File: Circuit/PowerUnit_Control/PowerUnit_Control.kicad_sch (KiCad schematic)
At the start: 25 parts, among them J1 Conn_01x02_Pin, J10 Conn_01x02_Pin, J11 Conn_01x02_Pin, J2 Conn_01x02_Pin, J3 Conn_01x07_Socket, J4 Conn_01x02_Pin, J5 Conn_01x02_Pin, J6 Conn_01x07_Socket, J7 Conn_01x02_Pin, J8 Conn_01x02_Pin, J9 Conn_01x07_Socket, SW1 SW_Toggle_DPDT

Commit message: 制御電源基板が完成
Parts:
- removed J6, J9: Conn_01x07_Socket, OU_Power:YDS512F-Unit, symbol Connector:Conn_01x07_Socket
- removed R6: 12k, Resistor_THT:R_Axial_DIN0207_L6.3mm_D2.5mm_P2.54mm_Vertical, symbol Device:R
- removed R7: 1.5k, Resistor_THT:R_Axial_DIN0207_L6.3mm_D2.5mm_P2.54mm_Vertical, symbol Device:R
- removed RV2, RV3: 20k, OU_Reg:TRIM_3296W-1-250, symbol Device:R_Potentiometer_Trim
- removed SW1: SW_Toggle_DPDT, OU_Switch:1MD6-T1-B1-M1-Q-N-S, symbol Switch:SW_Push_DPDT
- added C3, C7: 10u, Capacitor_SMD:C_1206_3216Metric, symbol Device:C
- added C4, C8: 0.1u, Capacitor_SMD:C_0603_1608Metric, symbol Device:C
- added C5, C9: 4.7u, Capacitor_SMD:C_0805_2012Metric, symbol Device:C
- added C6: 1000u, Capacitor_THT:CP_Radial_D16.0mm_P7.50mm, symbol Device:C_Polarized
- added D2, D3, D5: SS56C, OU_Diode:DIODE_SS56C-HF_CIP, symbol Device:D_Schottky
- added D4, D6: LED, LED_THT:LED_D5.0mm, symbol Device:LED
- added J6: Conn_01x02_Pin, OU_Conn:AMASS_XT30U-F, symbol Connector:Conn_01x02_Pin
- added J9: Conn_01x02_Pin, OU_Conn:Hirose_DF1EC-2P-2.5DSA_1x02_P2.5mm_Vertical, symbol Connector:Conn_01x02_Pin
- added U1: M78AR05-1, OU_Power:M78AR05-1, symbol Regulator_Linear:LM7812_TO220
- added U2: M78AR033-1, OU_Power:M78AR033-1, symbol Regulator_Linear:LM7812_TO220
- C1: footprint Capacitor_THT:C_Disc_D6.0mm_W4.4mm_P5.00mm -> Capacitor_SMD:C_0603_1608Metric; MPN (none) -> C15849; MPN_URL https://akizukidenshi.com/catalog/g/g108150/ -> (none)
- C2: value 470u -> 1000u; footprint Capacitor_THT:CP_Radial_D10.0mm_P5.00mm -> Capacitor_THT:CP_Radial_D16.0mm_P7.50mm; MPN_URL https://akizukidenshi.com/catalog/g/g102719/ -> https://akizukidenshi.com/catalog/g/g108442/
- J1: footprint OU_Conn:AMASS_XT60PW-M -> OU_Conn:AMASS_XT30PW-M; MPN (none) -> XT30PW-M; MPN_URL (none) -> https://akizukidenshi.com/catalog/g/g117949/
- J10, J11, J7, J8: footprint OU_Conn:AMASS_XT30U-F -> OU_Conn:Hirose_DF1EC-2P-2.5DSA_1x02_P2.5mm_Vertical; MPN XT30PW-M -> (none); MPN_URL https://akizukidenshi.com/catalog/g/g117949/ -> (none)
- R2, R3: footprint Resistor_THT:R_Axial_DIN0207_L6.3mm_D2.5mm_P2.54mm_Vertical -> Resistor_SMD:R_0603_1608Metric
- R4: value 12k -> 1k
- R5: value 1.5k -> 430
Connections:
- net at C1.1, J1.2 (Pin_2), R1.1: now also D2.2 (A), D3.2 (A), D5.2 (A); no longer C2.1, J3.1 (Pin_1), J3.2 (Pin_2)
- net at J10.2 (Pin_2), J11.2 (Pin_2): now also R5.1, C9.1, U2.3 (VO)
- net at J7.2 (Pin_2), J8.2 (Pin_2), R4.1: now also C5.1, J9.2 (Pin_2), U1.3 (VO)
- net at J3.5 (Pin_5), J3.6 (Pin_6), J4.2 (Pin_2)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: now also J2.2 (Pin_2), J6.2 (Pin_2)
- net at R4.2: now also D4.2 (A)
- net GNDPWR renamed GND
- net GND: now also C3.2, C4.2, C5.2, C6.2, C7.2, C8.2, C9.2, D4.1 (K), D6.1 (K), J6.1 (Pin_1), J9.1 (Pin_1), U1.2 (GND), U2.2 (GND); no longer R5.2
- new net: C2.1, C3.1, C4.1, D3.1 (K), U1.1 (VI)
- new net: C6.1, C7.1, C8.1, D5.1 (K), U2.1 (VI)
- new net: D2.1 (K), J3.1 (Pin_1), J3.2 (Pin_2)
- new net: D6.2 (A), R5.2
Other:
- note added: "3.3V電源1"
- note added: "3.3V電源2"
- note added: "3.3V電源LED"
- note added: "5V電源1"
- note added: "5V電源2"
- note added: "5V電源3"
- note added: "5V電源LED"
- note added: "リニアレギュレータっぽいですが、 ピン互換があるスイッチング レギュレータです"
- note added: "制御電源LED"
- note added: "汎用電源1"
- note added: "汎用電源2"
- note added: "汎用電源3"
- note removed: "サーボ汎用1.1"
- note removed: "サーボ汎用1.2"
- note removed: "サーボ汎用2.1"
- note removed: "サーボ汎用2.2"
- note removed: "サーボ汎用3.1"
- note removed: "サーボ汎用3.2"
- note removed: "駆動電源LED"

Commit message: 再度修正
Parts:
- added F1: 5A, OU_Fuse:FUC-03A, symbol Device:Fuse
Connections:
- net at C1.1, D2.2 (A), D3.2 (A)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: now also F1.2; no longer J1.2 (Pin_2)
- new net: F1.1, J1.2 (Pin_2)
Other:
- moved on the sheet: J1
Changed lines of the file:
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@@
 	(wire
 		(pts
-			(xy 19.05 44.45) (xy 19.05 100.33)
+			(xy 19.05 38.1) (xy 19.05 100.33)
 		)
 		(stroke
@@
 	(wire
 		(pts
+			(xy 21.59 46.99) (xy 21.59 49.53)
+		)
+		(stroke
+			(width 0)
+			(type default)
+		)
+	)
+	(wire
+		(pts
 			(xy 72.39 81.28) (xy 71.12 81.28)
 		)
@@
 	(wire
 		(pts
-			(xy 21.59 44.45) (xy 21.59 49.53)
+			(xy 21.59 38.1) (xy 21.59 39.37)
 		)
 		(stroke
@@
 	(symbol
 		(lib_id "Connector:Conn_01x02_Pin")
-		(at 19.05 39.37 90)
+		(at 19.05 33.02 90)
 		(mirror x)
 		(unit 1)
@@
 		(dnp no)
 		(property "Reference" "J1"
-			(at 20.066 34.798 90)
+			(at 20.066 28.448 90)
 			(show_name no)
 			(do_not_autoplace no)
@@
 		)
 		(property "Value" "Conn_01x02_Pin"
-			(at 20.32 37.846 90)
+			(at 20.32 31.496 90)
 			(show_name no)
 			(do_not_autoplace no)
@@
 		)
 		(property "Footprint" "OU_Conn:AMASS_XT30PW-M"
-			(at 19.05 39.37 0)
+			(at 19.05 33.02 0)
 			(hide yes)
 			(show_name no)
@@
 		)
 		(property "Datasheet" ""
-			(at 19.05 39.37 0)
+			(at 19.05 33.02 0)
 			(hide yes)
 			(show_name no)
@@
 		)
 		(property "Description" "Generic connector, single row, 01x02, script generated"
-			(at 19.05 39.37 0)
+			(at 19.05 33.02 0)
 			(hide yes)
 			(show_name no)
@@
 		)
 		(property "Fuse" ""
-			(at 19.05 39.37 0)
+			(at 19.05 33.02 0)
 			(hide yes)
 			(show_name no)
@@
 		)
 		(property "MPN" "XT30PW-M"
-			(at 19.05 39.37 0)
+			(at 19.05 33.02 0)
 			(hide yes)
 			(show_name no)
@@
 		)
 		(property "MPN_URL" "https://akizukidenshi.com/catalog/g/g117949/"
-			(at 19.05 39.37 0)
+			(at 19.05 33.02 0)
 			(hide yes)
 			(show_name no)
@@
 					(unit 1)
 				)
+			)
+		)
+	)
+	(symbol
+		(lib_id "Device:Fuse")
+		(at 21.59 43.18 0)
+		(unit 1)
+		(body_style 1)
+		(exclude_from_sim no)
+		(in_bom yes)
+		(on_board yes)
+		(in_pos_files yes)
+		(dnp no)
+		(fields_autoplaced yes)
+		(property "Reference" "F1"
+			(at 24.13 41.9099 0)
+			(show_name no)
+			(do_not_autoplace no)
+			(effects
+				(font
+					(size 1.27 1.27)
+				)
+				(justify left)
+			)
+		)
+		(property "Value" "5A"
+			(at 24.13 44.4499 0)
+			(show_name no)
+			(do_not_autoplace no)
+			(effects
+				(font
+					(size 1.27 1.27)
+				)
+				(justify left)
+			)
+		)
+		(property "Footprint" "OU_Fuse:FUC-03A"
+			(at 19.812 43.18 90)
+			(hide yes)
+			(show_name no)
+			(do_not_autoplace no)
+			(effects
+				(font
+					(size 1.27 1.27)
+				)
+			)
+		)
+		(property "Datasheet" ""
+			(at 21.59 43.18 0)
+			(hide yes)
+			(show_name no)
+			(do_not_autoplace no)
+			(effects
+				(font
+					(size 1.27 1.27)
+				)
+			)
+		)
+		(property "Description" "Fuse"
+			(at 21.59 43.18 0)
+			(hide yes)
+			(show_name no)
+			(do_not_autoplace no)
+			(effects
+				(font
+					(size 1.27 1.27)
+				)
+			)
+		)
+		(property "MPN_URL" "https://akizukidenshi.com/catalog/g/g110521/, https://akizukidenshi.com/catalog/g/g107131/"
+			(at 21.59 43.18 0)
+			(hide yes)
+			(show_name no)
+			(do_not_autoplace no)
+			(effects
+				(font
+					(size 1.27 1.27)
+				)
+			)
+		)
+		(pin "1"
+		)
+		(pin "2"
+		)
+		(instances
+			(project "PowerUnit_Control"
+				(path "/94f453ed-3c09-4964-9db6-2f3edd4da60d"
+					(reference "F1")
+					(unit 1)
+				)

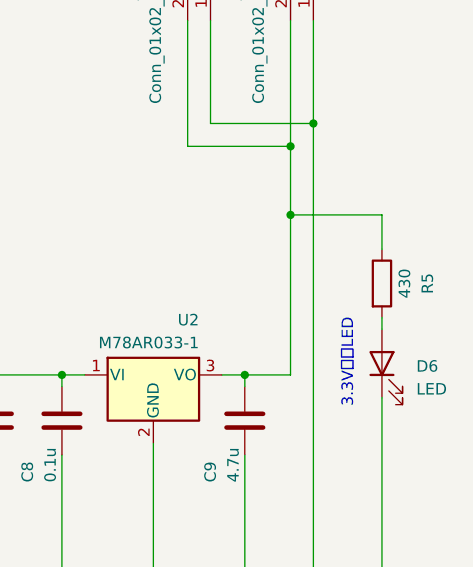
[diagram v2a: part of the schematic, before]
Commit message: 発注用データを用意 発注した
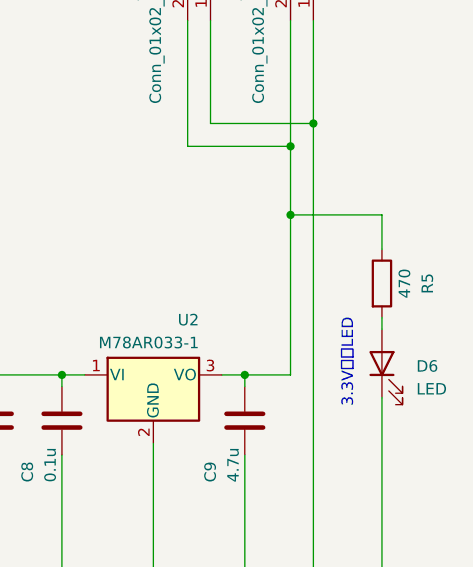
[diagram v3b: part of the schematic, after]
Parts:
- D1, D4, D6: MPN_URL (none) -> https://akizukidenshi.com/catalog/g/g111333/
- R1: MPN_URL (none) -> https://akizukidenshi.com/catalog/g/g125752/
- R4: MPN_URL (none) -> https://akizukidenshi.com/catalog/g/g125102/
- R5: value 430 -> 470; MPN_URL (none) -> https://akizukidenshi.com/catalog/g/g125471/
- U1: MPN_URL (none) -> https://akizukidenshi.com/catalog/g/g113536/
- U2: MPN_URL (none) -> https://akizukidenshi.com/catalog/g/g113535/
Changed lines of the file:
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@@
+			)
+		)
+		(property "MPN_URL" "https://akizukidenshi.com/catalog/g/g113536/"
+			(at 130.81 69.85 0)
+			(hide yes)
+			(show_name no)
+			(do_not_autoplace no)
+			(effects
+				(font
+					(size 1.27 1.27)
+				)
 			)
 		)
@@
 			)
 		)
+		(property "MPN_URL" "https://akizukidenshi.com/catalog/g/g111333/"
+			(at 154.94 68.58 90)
+			(hide yes)
+			(show_name no)
+			(do_not_autoplace no)
+			(effects
+				(font
+					(size 1.27 1.27)
+				)
+			)
+		)
 		(pin "1"
 		)
@@
 			)
 		)
+		(property "MPN_URL" "https://akizukidenshi.com/catalog/g/g125102/"
+			(at 154.94 59.69 90)
+			(hide yes)
+			(show_name no)
+			(do_not_autoplace no)
+			(effects
+				(font
+					(size 1.27 1.27)
+				)
+			)
+		)
 		(pin "1"
 		)
@@
 			)
 		)
-		(property "Value" "430"
+		(property "Value" "470"
 			(at 223.52 59.69 90)
 			(show_name no)
@@
 		)
 		(property "Fuse" ""
+			(at 220.98 59.69 90)
+			(hide yes)
+			(show_name no)
+			(do_not_autoplace no)
+			(effects
+				(font
+					(size 1.27 1.27)
+				)
+			)
+		)
+		(property "MPN_URL" "https://akizukidenshi.com/catalog/g/g125471/"
 			(at 220.98 59.69 90)
 			(hide yes)
@@
 			)
 		)
+		(property "MPN_URL" "https://akizukidenshi.com/catalog/g/g111333/"
+			(at 33.02 63.5 90)
+			(hide yes)
+			(show_name no)
+			(do_not_autoplace no)
+			(effects
+				(font
+					(size 1.27 1.27)
+				)
+			)
+		)
 		(pin "1"
 		)
@@
 			)
 		)
+		(property "MPN_URL" "https://akizukidenshi.com/catalog/g/g113535/"
+			(at 195.58 69.85 0)
+			(hide yes)
+			(show_name no)
+			(do_not_autoplace no)
+			(effects
+				(font
+					(size 1.27 1.27)
+				)
+			)
+		)
 		(pin "3"
 		)
@@
 		)
 		(property "Fuse" ""
+			(at 33.02 54.61 90)
+			(hide yes)
+			(show_name no)
+			(do_not_autoplace no)
+			(effects
+				(font
+					(size 1.27 1.27)
+				)
+			)
+		)
+		(property "MPN_URL" "https://akizukidenshi.com/catalog/g/g125752/"
 			(at 33.02 54.61 90)
 			(hide yes)
@@
 			(at 220.98 68.58 90)
 			(hide yes)
+			(show_name no)
+			(do_not_autoplace no)
+			(effects
+				(font
+					(size 1.27 1.27)
+				)
+			)
+		)
+		(property "MPN_URL" "https://akizukidenshi.com/catalog/g/g111333/"
+			(at 220.98 68.58 90)
+			(hide yes)
